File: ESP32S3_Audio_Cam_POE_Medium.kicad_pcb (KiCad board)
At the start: 2 copper layers, 97.8 x 71.1 mm, 238 parts, among them CN1 PJ-316C-6A, J1 Connector, USB-TYPE-C-16P, J10 Conn_01x02, J11 Conn_01x02, J12 Conn_01x03, J13 Conn_01x03, J14 Conn_01x03, J15 Conn_01x03, J16 Conn_01x03, J17 Conn_01x02, J18 Conn_01x02, J19 Conn_01x02, J2 Conn_01x20_Pin, J3 Conn_01x20_Pin, J4 Conn_01x02, J5 Conn_01x02, J6 Conn_01x02, J7 Conn_01x02, J8 Conn_01x02, J9 Conn_01x02, Q1 AO3401A, Q2 AO3401A, Q3 AO3401A, Q4 AO3401A, Q5 AO3401A, Q6 AO3401A, Q7 AO3401A, U1 MT9221CT-06BR5, U10 DS18B20U(UMW), U2 USBLC6-2SC6, U3 TM1637, U4 MAX98357AETE+T, U5 ICS-43434, U6 ICS-43434, U7 ESP32-S3, U8 AXP2101, U9 W25Q128JVSIQ, Y1 40MHz, 15pF, Y2 32.768KHz

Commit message: Changed input power from 3.3V to 5V.
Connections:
- C3 pad 1: VBUS+3V3 -> Vsys_5V
- J2 pad 1: unconnected-(J2-Pin_1-Pad1) -> V-USB
- J2 pad 2: unconnected-(J2-Pin_2-Pad2) -> Vsys_5V
- J2 pad 4: unconnected-(J2-Pin_4-Pad4) -> 3V3-prim-EN
- J2 pad 5: VBUS+3V3 -> 3V3-primary
- U1 pad 3: VBUS+3V3 -> Vsys_5V
- U1 pad 4: VBUS+3V3 -> Vsys_5V
- U1 pad 8: VBUS+3V3 -> Vsys_5V
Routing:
- net Vsys_5V: track 0.00 -> 28.5 mm, vias 0 -> 2
- net VBUS+3V3: track 18.0 -> 0.00 mm, vias 2 -> 0
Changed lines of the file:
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@@
 	(net 107 "Net-(D8-Pad2)")
 	(net 108 "Net-(D9-A)")
-	(net 109 "unconnected-(J2-Pin_4-Pad4)")
-	(net 110 "unconnected-(J2-Pin_2-Pad2)")
+	(net 109 "Vsys_5V")
+	(net 110 "3V3-prim-EN")
 	(net 111 "unconnected-(J2-Pin_11-Pad11)")
 	(net 112 "/2USB_CC1")
@@
 	(net 116 "/2USB_PRT_D+")
 	(net 117 "unconnected-(J1-SBU2-PadB8)")
-	(net 118 "unconnected-(J2-Pin_1-Pad1)")
+	(net 118 "V-USB")
 	(net 119 "Net-(J7-Pin_1)")
 	(net 120 "Net-(J5-Pin_1)")
@@
 	(net 213 "unconnected-(U10-NC-Pad5)")
 	(net 214 "unconnected-(U10-NC-Pad7)")
-	(net 215 "VBUS+3V3")
+	(net 215 "3V3-primary")
 	(net 216 "Vdrive2")
 	(net 217 "unconnected-(U10-NC-Pad6)")
@@
 			(layers "F.Cu" "F.Mask" "F.Paste")
 			(roundrect_rratio 0.25)
-			(net 215 "VBUS+3V3")
+			(net 109 "Vsys_5V")
 			(pintype "passive")
 		)
@@
 			(size 0.574 2.0355)
 			(layers "F.Cu" "F.Mask" "F.Paste")
-			(net 215 "VBUS+3V3")
+			(net 109 "Vsys_5V")
 			(pinfunction "IP-")
 			(pintype "unspecified")
@@
 			(size 0.574 2.0355)
 			(layers "F.Cu" "F.Mask" "F.Paste")
-			(net 215 "VBUS+3V3")
+			(net 109 "Vsys_5V")
 			(pinfunction "IP-")
 			(pintype "unspecified")
@@
 			(size 0.574 2.0355)
 			(layers "F.Cu" "F.Mask" "F.Paste")
-			(net 215 "VBUS+3V3")
+			(net 109 "Vsys_5V")
 			(pinfunction "VCC")
 			(pintype "unspecified")
@@
 			(layers "*.Cu" "*.Mask")
 			(remove_unused_layers no)
-			(net 118 "unconnected-(J2-Pin_1-Pad1)")
+			(net 118 "V-USB")
 			(pinfunction "Pin_1")
-			(pintype "passive+no_connect")
+			(pintype "passive")
 		)
 		(pad "2" thru_hole circle
@@
 			(layers "*.Cu" "*.Mask")
 			(remove_unused_layers no)
-			(net 110 "unconnected-(J2-Pin_2-Pad2)")
+			(net 109 "Vsys_5V")
 			(pinfunction "Pin_2")
-			(pintype "passive+no_connect")
+			(pintype "passive")
 		)
 		(pad "3" thru_hole circle
@@
 			(layers "*.Cu" "*.Mask")
 			(remove_unused_layers no)
-			(net 109 "unconnected-(J2-Pin_4-Pad4)")
+			(net 110 "3V3-prim-EN")
 			(pinfunction "Pin_4")
-			(pintype "passive+no_connect")
+			(pintype "passive")
 		)
 		(pad "5" thru_hole circle
@@
 			(layers "*.Cu" "*.Mask")
 			(remove_unused_layers no)
-			(net 215 "VBUS+3V3")
+			(net 215 "3V3-primary")
 			(pinfunction "Pin_5")
 			(pintype "passive")
@@
 	)
 	(segment
+		(start 87.783 158.75)
+		(end 84.981 158.75)
+		(width 0.2032)
+		(layer "F.Cu")
+		(net 109)
+	)
+	(segment
+		(start 92.075 156.21)
+		(end 91.567 156.718)
+		(width 0.2032)
+		(layer "F.Cu")
+		(net 109)
+	)
+	(segment
+		(start 84.981 158.75)
+		(end 84.836 158.895)
+		(width 0.2032)
+		(layer "F.Cu")
+		(net 109)
+	)
+	(segment
+		(start 91.567 156.718)
+		(end 91.567 157.48)
+		(width 0.2032)
+		(layer "F.Cu")
+		(net 109)
+	)
+	(segment
+		(start 92.202 158.115)
+		(end 100.66925 158.115)
+		(width 0.2032)
+		(layer "F.Cu")
+		(net 109)
+	)
+	(segment
+		(start 91.567 157.48)
+		(end 92.202 158.115)
+		(width 0.2032)
+		(layer "F.Cu")
+		(net 109)
+	)
+	(segment
+		(start 93.319 156.21)
+		(end 92.075 156.21)
+		(width 0.2032)
+		(layer "F.Cu")
+		(net 109)
+	)
+	(segment
+		(start 100.66925 158.115)
+		(end 105.86135 152.9229)
+		(width 0.2032)
+		(layer "F.Cu")
+		(net 109)
+	)
+	(segment
+		(start 87.783 158.75)
+		(end 87.783 160.02)
+		(width 0.2032)
+		(layer "F.Cu")
+		(net 109)
+	)
+	(segment
+		(start 91.567 156.718)
+		(end 91.694 156.718)
+		(width 0.2032)
+		(layer "F.Cu")
+		(net 109)
+	)
+	(segment
+		(start 87.783 158.75)
+		(end 89.408 158.75)
+		(width 0.2032)
+		(layer "F.Cu")
+		(net 109)
+	)
+	(via
+		(at 89.408 158.75)
+		(size 0.6)
+		(drill 0.3)
+		(layers "F.Cu" "B.Cu")
+		(free yes)
+		(net 109)
+	)
+	(via
+		(at 91.567 156.718)
+		(size 0.6)
+		(drill 0.3)
+		(layers "F.Cu" "B.Cu")
+		(free yes)
+		(net 109)
+	)
+	(segment
+		(start 91.44 156.718)
+		(end 91.567 156.718)
+		(width 0.2032)
+		(layer "B.Cu")
+		(net 109)
+	)
+	(segment
+		(start 89.408 158.75)
+		(end 91.44 156.718)
+		(width 0.2032)
+		(layer "B.Cu")
+		(net 109)
+	)
+	(segment
 		(start 87.61 131.27)
 		(end 87.61 132.395)
@@
 	)
 	(segment
-		(start 87.783 158.75)
-		(end 84.981 158.75)
-		(width 0.2032)
-		(layer "F.Cu")
-		(net 215)
-	)
-	(segment
-		(start 98.24135 152.9229)
-		(end 98.24135 154.23465)
-		(width 0.2032)
-		(layer "F.Cu")
-		(net 215)
-	)
-	(segment
-		(start 92.075 156.21)
-		(end 91.567 156.718)
-		(width 0.2032)
-		(layer "F.Cu")
-		(net 215)
-	)
-	(segment
-		(start 84.981 158.75)
-		(end 84.836 158.895)
-		(width 0.2032)
-		(layer "F.Cu")
-		(net 215)
-	)
-	(segment
-		(start 96.266 156.21)
-		(end 93.319 156.21)
-		(width 0.2032)
-		(layer "F.Cu")
-		(net 215)
-	)
-	(segment
-		(start 93.319 156.21)
-		(end 92.075 156.21)
-		(width 0.2032)
-		(layer "F.Cu")
-		(net 215)
-	)
-	(segment
-		(start 98.24135 154.23465)
-		(end 96.266 156.21)
-		(width 0.2032)
-		(layer "F.Cu")
-		(net 215)
-	)
-	(segment
-		(start 87.783 158.75)
-		(end 87.783 160.02)
-		(width 0.2032)
-		(layer "F.Cu")
-		(net 215)
-	)
-	(segment
-		(start 91.567 156.718)
-		(end 91.694 156.718)
-		(width 0.2032)
-		(layer "F.Cu")
-		(net 215)
-	)
-	(segment
-		(start 87.783 158.75)
-		(end 89.408 158.75)
-		(width 0.2032)
-		(layer "F.Cu")
-		(net 215)
-	)
-	(via
-		(at 89.408 158.75)
-		(size 0.6)
-		(drill 0.3)
-		(layers "F.Cu" "B.Cu")
-		(net 215)
-	)
-	(via
-		(at 91.567 156.718)
-		(size 0.6)
-		(drill 0.3)
-		(layers "F.Cu" "B.Cu")
-		(net 215)
-	)
-	(segment
-		(start 91.44 156.718)
-		(end 91.567 156.718)
-		(width 0.2032)
-		(layer "B.Cu")
-		(net 215)
-	)
-	(segment
-		(start 89.408 158.75)
-		(end 91.44 156.718)
-		(width 0.2032)
-		(layer "B.Cu")
-		(net 215)
-	)
-	(segment

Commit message: flipped RC servo headers to back side.
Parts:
- J12, J14, J15, J16: moved to B.Cu
- turned J12 to -90 degrees
- turned J14 to -90 degrees
- turned J15 to -90 degrees
- turned J16 to -90 degrees
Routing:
- net COM: vias 253 -> 250
- net /RC.VDD: vias 0 -> 3

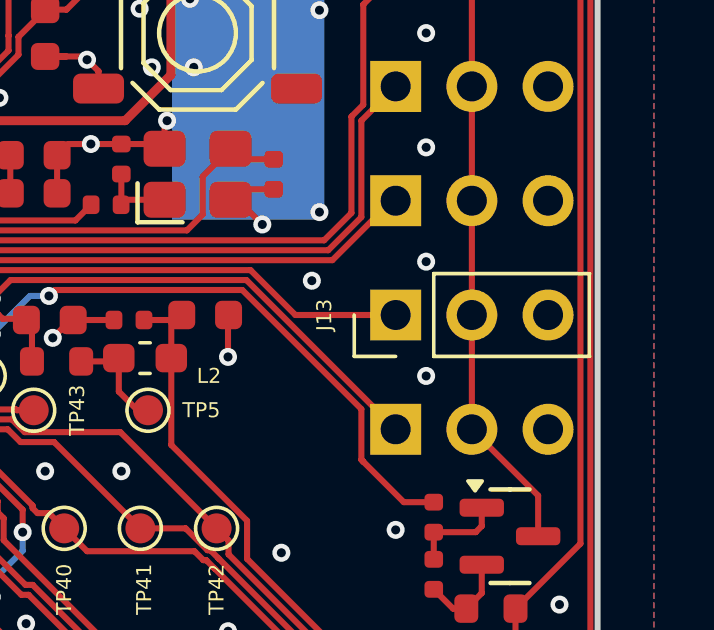
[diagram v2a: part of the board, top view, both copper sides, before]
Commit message: flipped RC servo headers to back side.
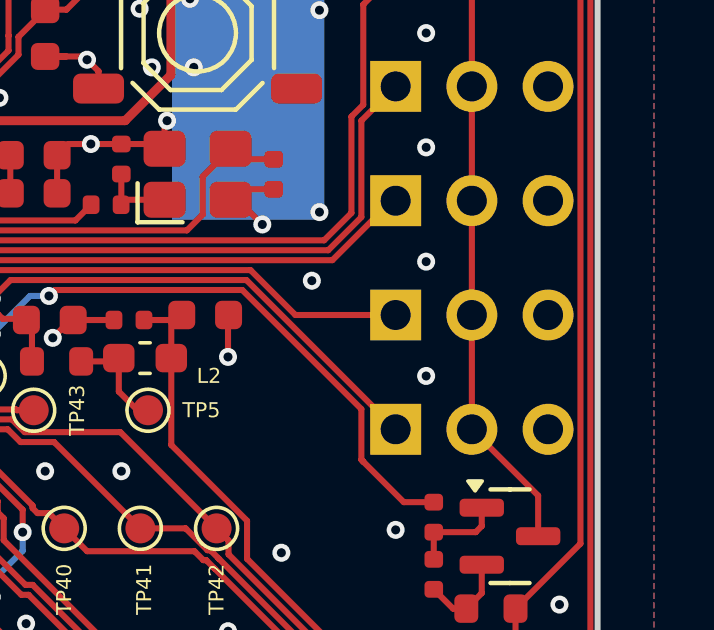
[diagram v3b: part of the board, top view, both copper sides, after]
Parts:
- J13: moved to B.Cu
- turned J13 to -90 degrees
